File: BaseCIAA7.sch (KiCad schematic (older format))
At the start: 17 parts, among them J10 Conn_02x12_Odd_Even, J13 Conn_02x05_Odd_Even, J18 Conn_02x05_Odd_Even, J7 Conn_02x12_Odd_Even, J8 Conn_02x20_Counter_Clockwise, J9 Conn_02x12_Odd_Even

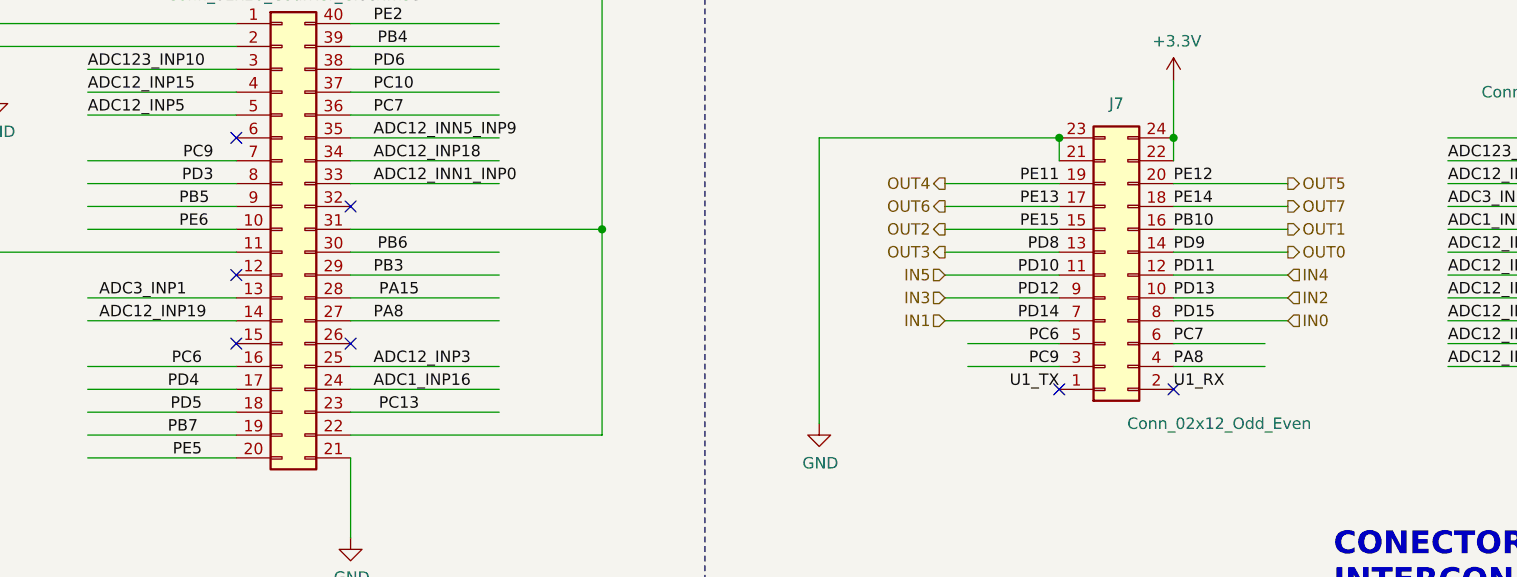
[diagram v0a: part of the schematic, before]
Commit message: Ruteo Parcial-Replanteo Esquematico pafa favorecer ruteo v4
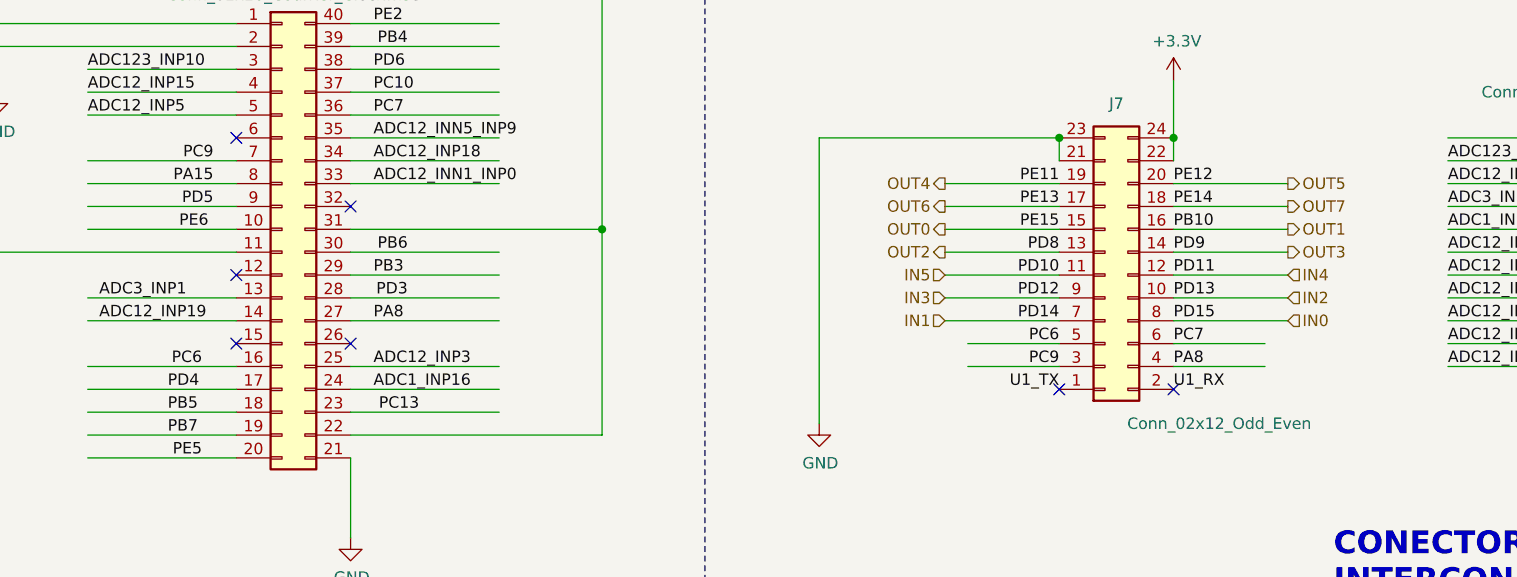
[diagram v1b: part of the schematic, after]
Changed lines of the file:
@@
 Wire Wire Line
 	5900 4400 5400 4400
-Text HLabel 6900 4700 2    50   Output ~ 0
+Text HLabel 5400 4600 0    50   Output ~ 0
 OUT0
 Text HLabel 6900 4600 2    50   Output ~ 0
 OUT1
-Text HLabel 5400 4600 0    50   Output ~ 0
+Text HLabel 5400 4700 0    50   Output ~ 0
 OUT2
-Text HLabel 5400 4700 0    50   Output ~ 0
+Text HLabel 6900 4700 2    50   Output ~ 0
 OUT3
 Text HLabel 5400 4400 0    50   Output ~ 0
@@
 	1    0    0    -1
 $EndComp
-Text Label 2150 5400 2    50   ~ 0
+Text Label 2200 4500 2    50   ~ 0
 PD5
 Text Label 3050 3800 2    50   ~ 0
@@
 Text Label 2900 4800 0    50   ~ 0
 PB3
-Text Label 2050 4500 0    50   ~ 0
+Text Label 2000 5400 0    50   ~ 0
 PB5
 Text Label 2000 5500 0    50   ~ 0
@@
 Wire Wire Line
 	10400 5300 10800 5300
-Text Label 3100 4900 2    50   ~ 0
+Text Label 2200 4400 2    50   ~ 0
 PA15
-Text Label 2200 4400 2    50   ~ 0
+Text Label 3050 4900 2    50   ~ 0
 PD3
 Wire Wire Line

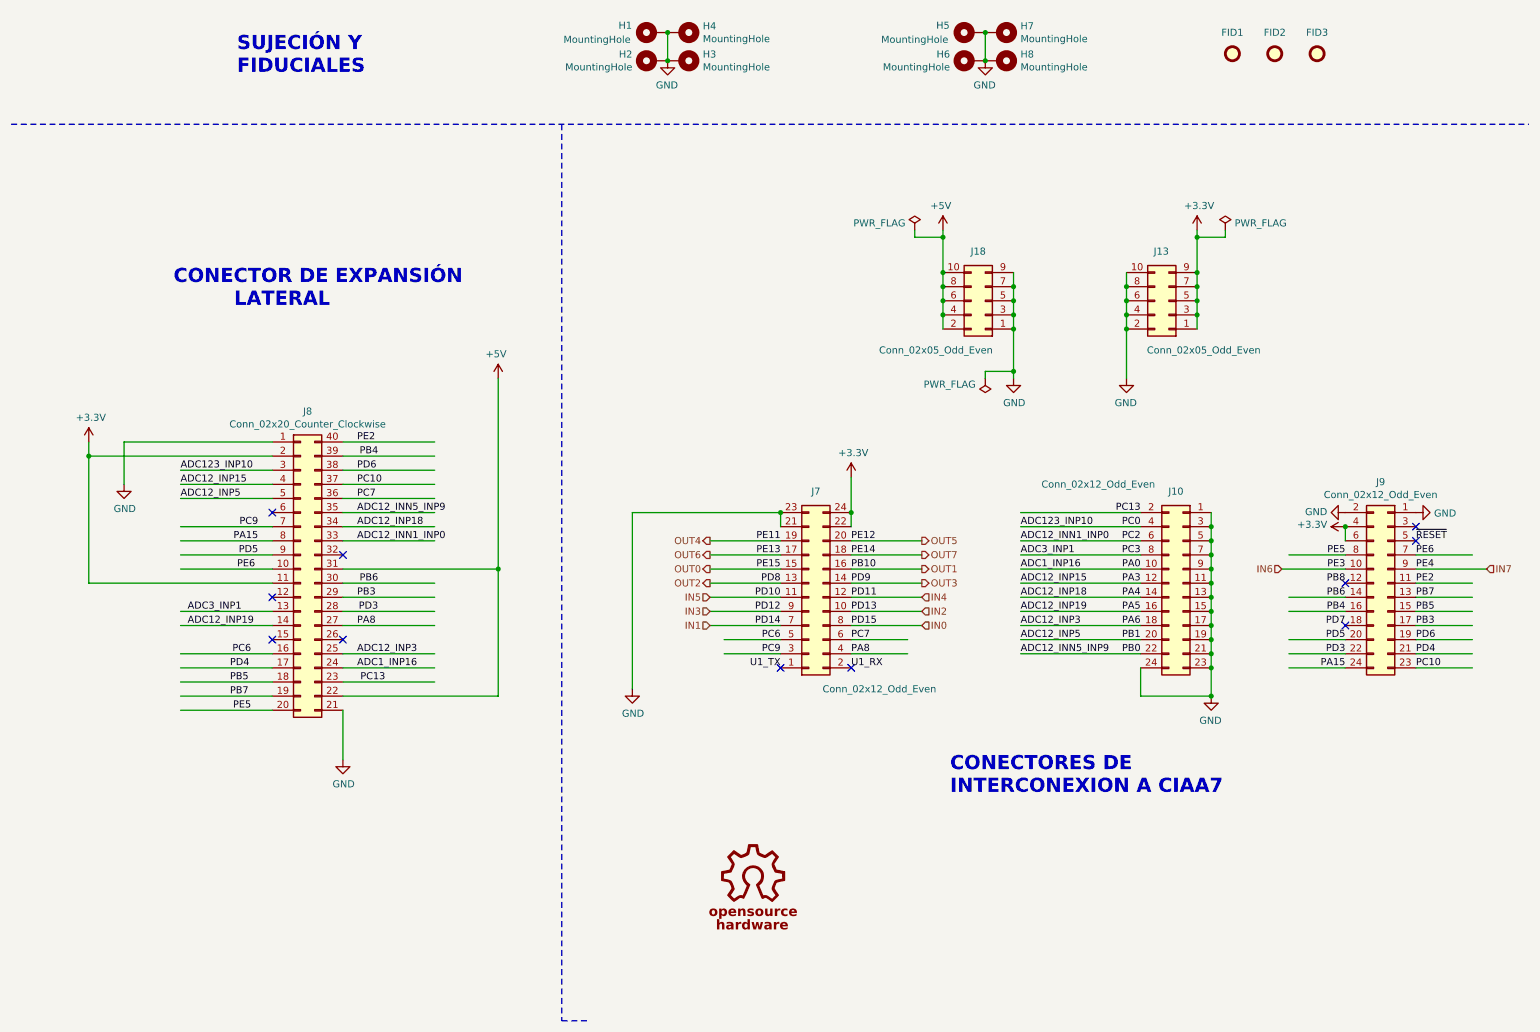
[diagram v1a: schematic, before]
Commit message: Ruteo Casi terminado (faltan planos de masa)
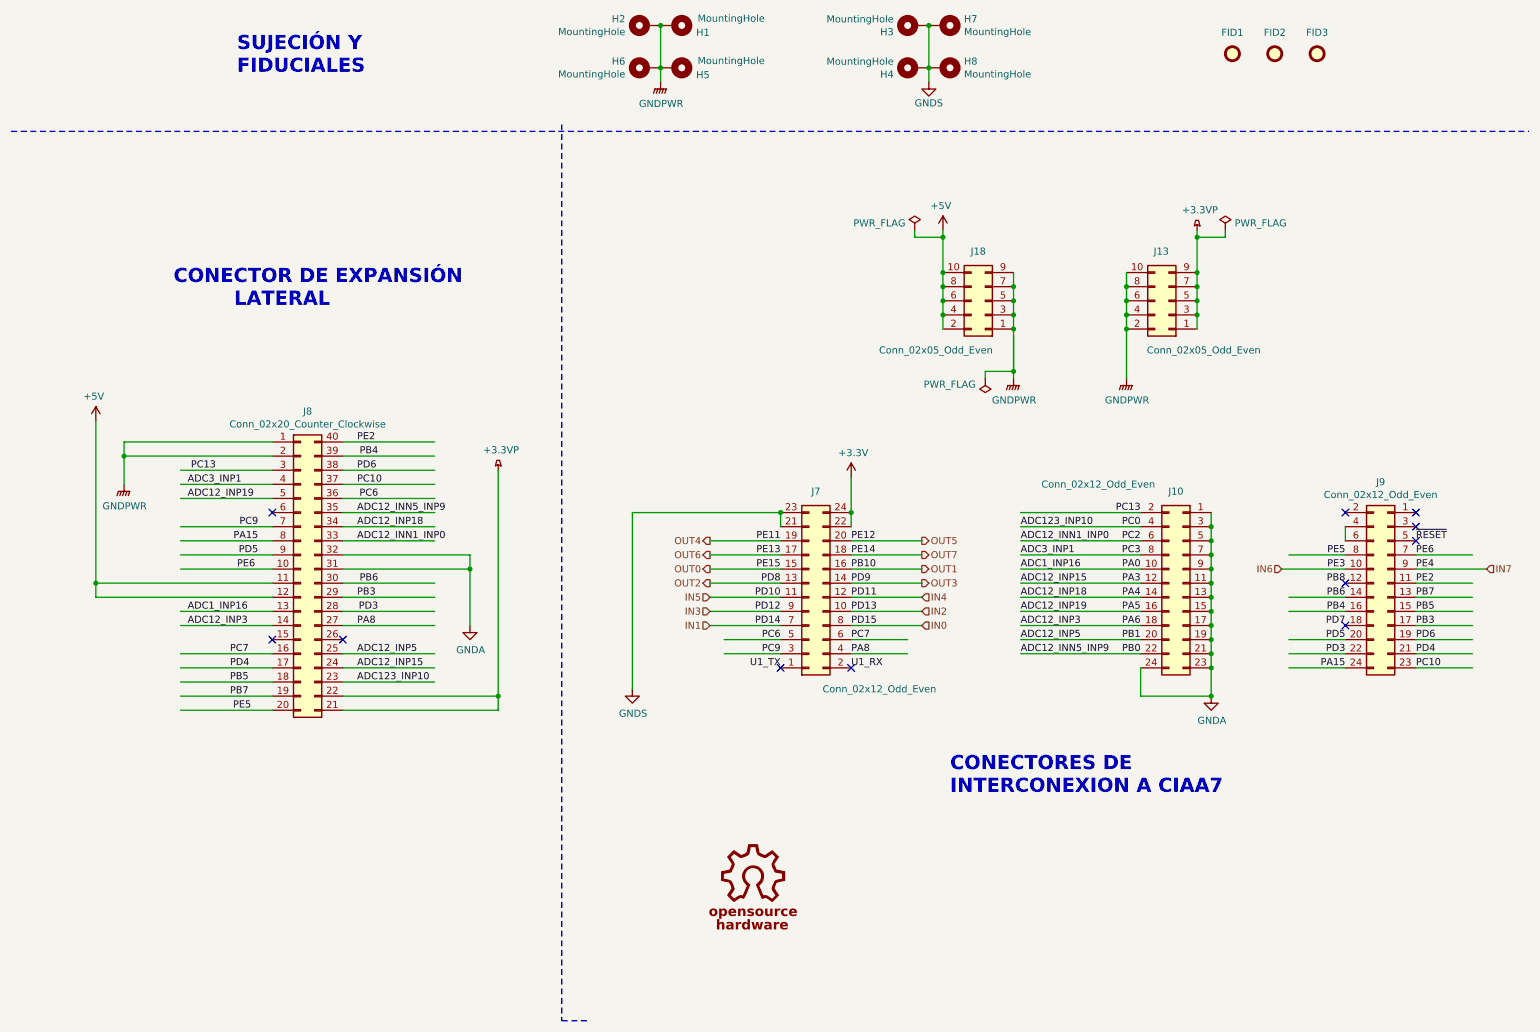
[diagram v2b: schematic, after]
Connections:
- net labels added: +3.3VP, GNDA, GNDPWR, GNDS
- net labels removed: GND
- wire segments 136 -> 144
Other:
- moved on the sheet: H1, H2, H3, H4, H5, H6, H7, H8
